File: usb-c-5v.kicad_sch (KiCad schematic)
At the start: 9 parts, among them J2 USB_B_Micro, U2 AP2112K-3.3

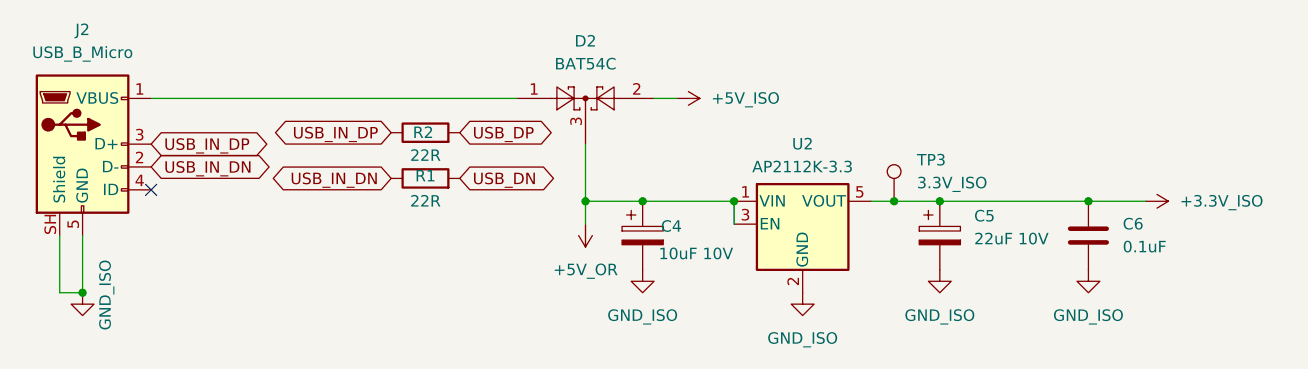
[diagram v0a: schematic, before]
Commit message: Update annotations, fixed font sizes.
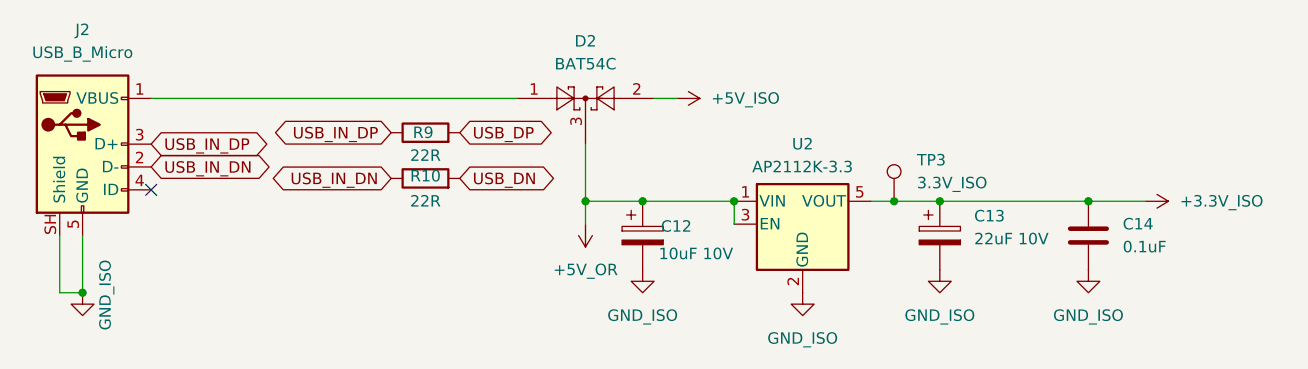
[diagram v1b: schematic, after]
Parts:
- renumbered C4 to C12, C5 to C13, C6 to C14, R1 to R10, R2 to R9
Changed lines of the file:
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@@
 		(in_pos_files yes)
 		(dnp no)
-		(property "Reference" "R2"
+		(property "Reference" "R9"
 			(at 83.566 44.45 90)
 			(show_name no)
@@
 			(project "barn-blinds-controller"
 				(path "/aa90962a-81b9-423d-8acd-c4e83fa798bb/52efa7a4-2a50-492f-ba41-4a5be1c27b4c"
-					(reference "R2")
+					(reference "R9")
 					(unit 1)
 				)
@@
 		(dnp no)
 		(fields_autoplaced yes)
-		(property "Reference" "C5"
+		(property "Reference" "C13"
 			(at 144.78 53.7209 0)
 			(show_name no)
@@
 			(project "barn-blinds-controller"
 				(path "/aa90962a-81b9-423d-8acd-c4e83fa798bb/52efa7a4-2a50-492f-ba41-4a5be1c27b4c"
-					(reference "C5")
+					(reference "C13")
 					(unit 1)
 				)
@@
 		(in_pos_files yes)
 		(dnp no)
-		(property "Reference" "R1"
+		(property "Reference" "R10"
 			(at 83.82 49.276 90)
 			(show_name no)
@@
 			(project "barn-blinds-controller"
 				(path "/aa90962a-81b9-423d-8acd-c4e83fa798bb/52efa7a4-2a50-492f-ba41-4a5be1c27b4c"
-					(reference "R1")
+					(reference "R10")
 					(unit 1)
 				)
@@
 		(in_pos_files yes)
 		(dnp no)
-		(property "Reference" "C4"
+		(property "Reference" "C12"
 			(at 109.982 54.864 0)
 			(show_name no)
@@
 			(project "barn-blinds-controller"
 				(path "/aa90962a-81b9-423d-8acd-c4e83fa798bb/52efa7a4-2a50-492f-ba41-4a5be1c27b4c"
-					(reference "C4")
+					(reference "C12")
 					(unit 1)
 				)
@@
 		(dnp no)
 		(fields_autoplaced yes)
-		(property "Reference" "C6"
+		(property "Reference" "C14"
 			(at 161.29 54.6099 0)
 			(show_name no)
@@
 			(project "barn-blinds-controller"
 				(path "/aa90962a-81b9-423d-8acd-c4e83fa798bb/52efa7a4-2a50-492f-ba41-4a5be1c27b4c"
-					(reference "C6")
-					(unit 1)
-				)
+					(reference "C14")
+					(unit 1)
+				)
